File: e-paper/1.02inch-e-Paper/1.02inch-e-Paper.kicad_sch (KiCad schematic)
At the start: 21 parts, among them J1 Conn_01x06_Pin, J2 Conn_01x03_Pin

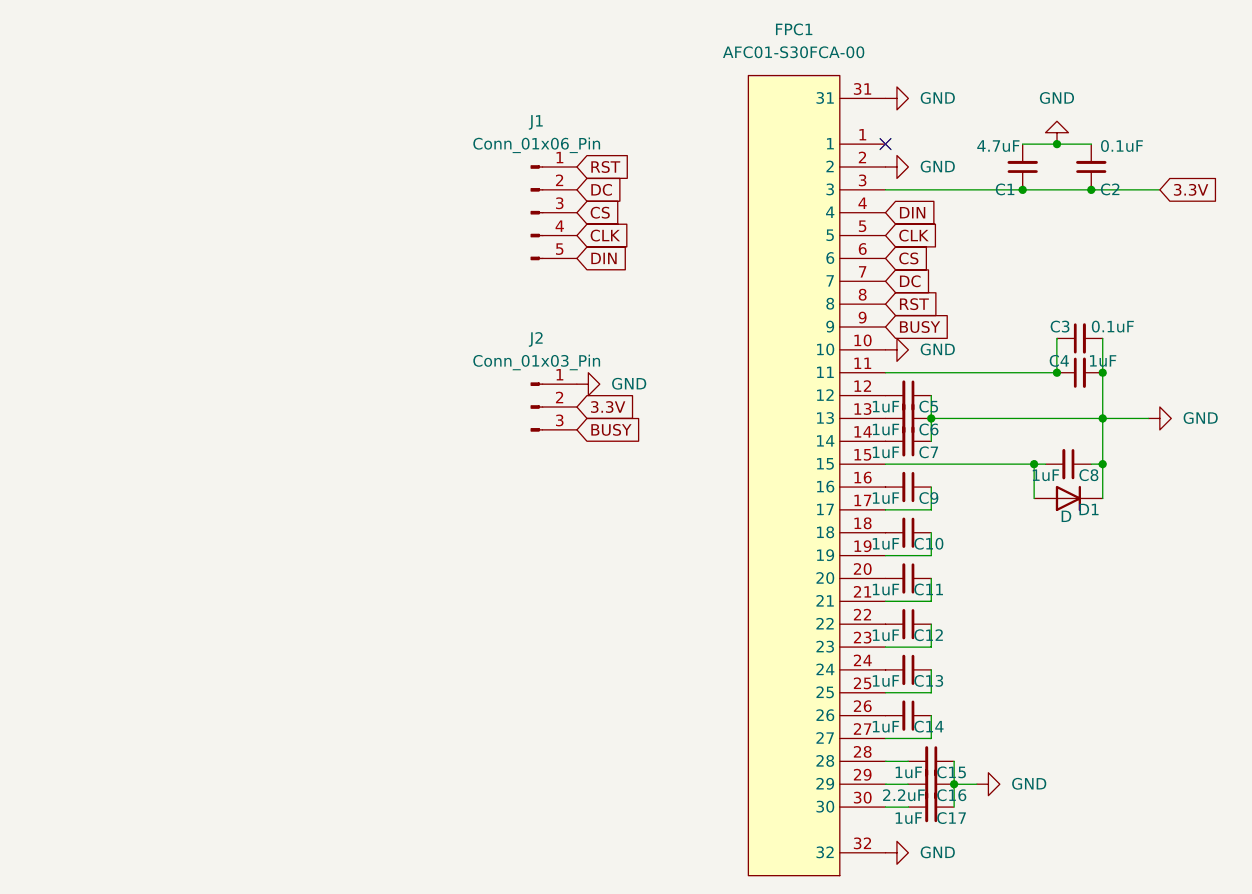
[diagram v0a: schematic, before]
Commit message: add RGB led in e-paper module
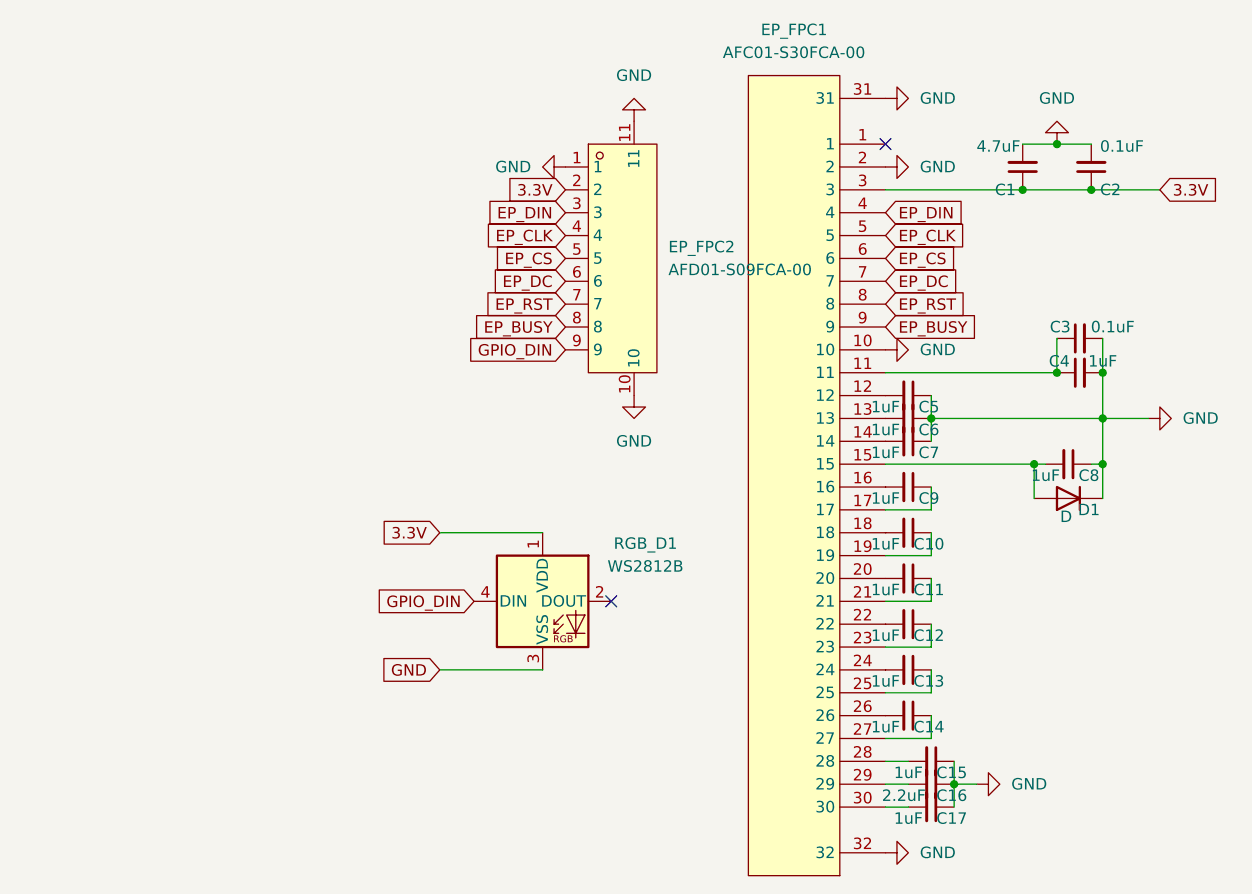
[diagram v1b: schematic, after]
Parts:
- removed J1: Conn_01x06_Pin, Connector_PinHeader_2.54mm:PinHeader_1x05_P2.54mm_Vertical, symbol Connector:Conn_01x05_Pin
- removed J2: Conn_01x03_Pin, Connector_PinHeader_2.54mm:PinHeader_1x03_P2.54mm_Vertical, symbol Connector:Conn_01x03_Pin
- added EP_FPC2: AFD01-S09FCA-00, ErgoCai.pretty:FPC-SMD_9P-P0.50_JS_AFD01-S09FCA-00, symbol ErgoCai:AFD01-S09FCA-00
- added RGB_D1: WS2812B, ErgoCai.pretty:LED_WS2812B_PLCC4_5.0x5.0mm_P3.2mm, symbol LED:WS2812B
- renumbered FPC1 to EP_FPC1
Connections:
- net 3.3V: now also EP_FPC2.2, RGB_D1.1 (VDD)
- net GND: now also EP_FPC2.1, EP_FPC2.10, EP_FPC2.11, RGB_D1.3 (VSS)
- net BUSY renamed EP_BUSY
- net EP_BUSY: now also EP_FPC2.8
- net CLK renamed EP_CLK
- net EP_CLK: now also EP_FPC2.4
- net CS renamed EP_CS
- net EP_CS: now also EP_FPC2.5
- net DC renamed EP_DC
- net EP_DC: now also EP_FPC2.6
- net DIN renamed EP_DIN
- net EP_DIN: now also EP_FPC2.3
- net RST renamed EP_RST
- net EP_RST: now also EP_FPC2.7
- new net GPIO_DIN: EP_FPC2.9, RGB_D1.4 (DIN)
- no-connect marks 1 -> 2

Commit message: use 10pin connector socket instead of 9
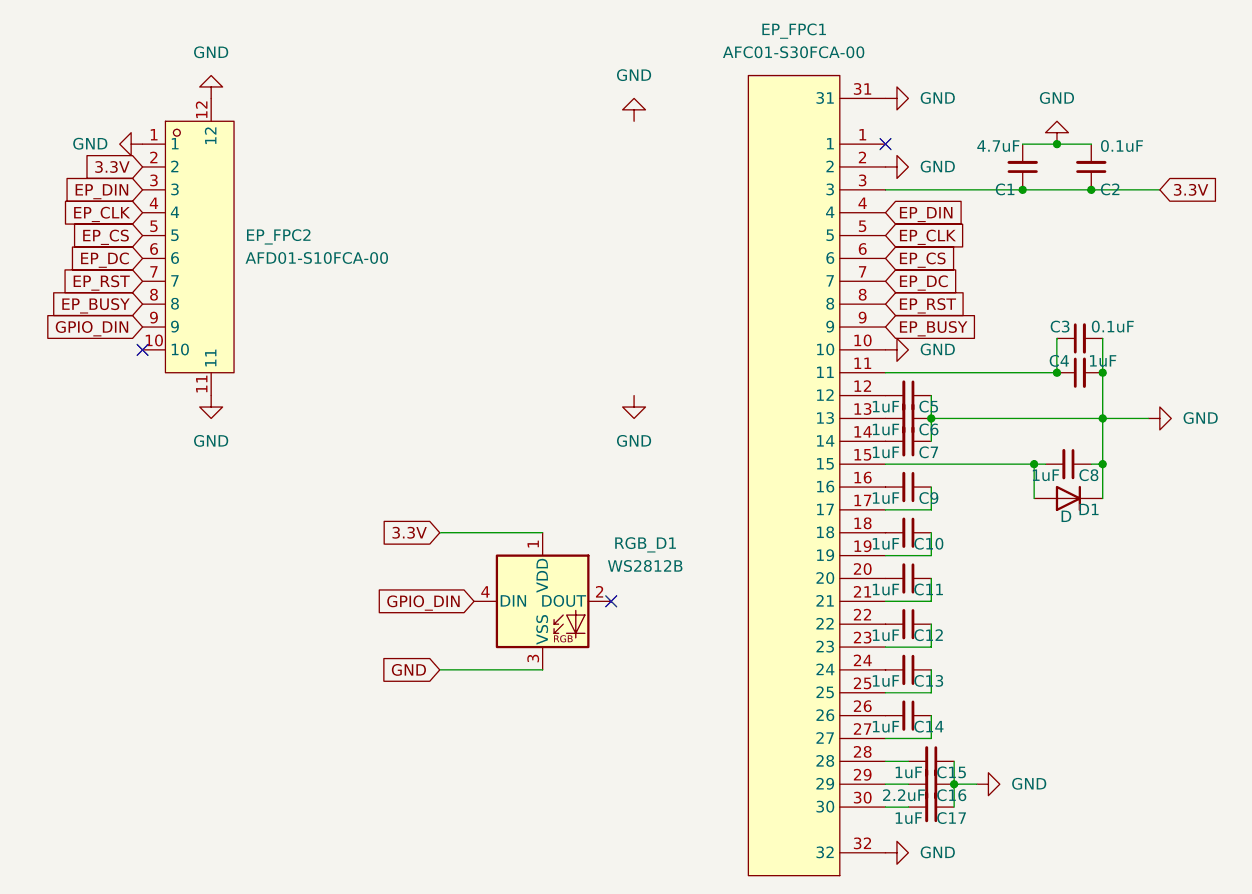
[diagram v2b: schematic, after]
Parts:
- removed EP_FPC2: AFD01-S09FCA-00, ErgoCai.pretty:FPC-SMD_9P-P0.50_JS_AFD01-S09FCA-00, symbol ErgoCai:AFD01-S09FCA-00
- added EP_FPC2: AFD01-S10FCA-00, easyeda2kicad:FPC-SMD_10P-P0.50_JS_AFD01-S10FCA-00, symbol ErgoCai:AFD01-S10FCA-00
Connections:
- net 3.3V: now also EP_FPC2.2
- net EP_BUSY: now also EP_FPC2.8
- net EP_CLK: now also EP_FPC2.4
- net EP_CS: now also EP_FPC2.5
- net EP_DC: now also EP_FPC2.6
- net EP_DIN: now also EP_FPC2.3
- net EP_RST: now also EP_FPC2.7
- net GND: now also EP_FPC2.1, EP_FPC2.11, EP_FPC2.12
- net GPIO_DIN: now also EP_FPC2.9
- no-connect marks 2 -> 3

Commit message: updat e-paper module
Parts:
- EP_FPC2: footprint easyeda2kicad:FPC-SMD_10P-P0.50_JS_AFD01-S10FCA-00 -> ErgoCai.pretty:FPC-SMD_10P-P0.50_JS_AFD01-S10FCA-00
- EP_RGB1: renamed from RGB_D1; footprint ErgoCai.pretty:LED_WS2812B_PLCC4_5.0x5.0mm_P3.2mm -> ErgoCai.pretty:LED-SMD_4P-L5.0-W5.0-TL_WS2812B-B
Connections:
- net 3.3V: now also EP_FPC2.9; no longer EP_FPC2.2
- net EP_BUSY: now also EP_FPC2.3; no longer EP_FPC2.8
- net EP_CLK: now also EP_FPC2.7; no longer EP_FPC2.4
- net EP_CS: now also EP_FPC2.6; no longer EP_FPC2.5
- net EP_DC: now also EP_FPC2.5; no longer EP_FPC2.6
- net EP_DIN: now also EP_FPC2.8; no longer EP_FPC2.3
- net EP_RST: now also EP_FPC2.4; no longer EP_FPC2.7
- net GPIO_DIN: now also EP_FPC2.2; no longer EP_FPC2.9
